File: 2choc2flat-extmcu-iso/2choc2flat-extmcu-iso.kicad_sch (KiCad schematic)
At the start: 142 parts, among them J1 Conn_01x09_Male, J2 Conn_01x05_Male, J3 Conn_01x09_Male, K1 KEYSW, K10 KEYSW, K11 KEYSW, K12 KEYSW, K13 KEYSW, K14 KEYSW, K15 KEYSW, K16 KEYSW, K17 KEYSW, K18 KEYSW, K19 KEYSW, K2 KEYSW, K20 KEYSW, K21 KEYSW, K22 KEYSW, K23 KEYSW, K24 KEYSW, K25 KEYSW, K26 KEYSW, K27 KEYSW, K28 KEYSW, K29 KEYSW, K29-1 KEYSW, K3 KEYSW, K30 KEYSW, K31 KEYSW, K32 KEYSW, K33 KEYSW, K34 KEYSW, K35 KEYSW, K36 KEYSW, K37 KEYSW, K38 KEYSW, K39 KEYSW, K4 KEYSW, K40 KEYSW, K41 KEYSW, K42 KEYSW, K43 KEYSW, K44 KEYSW, K45 KEYSW, K46 KEYSW, K47 KEYSW, K48 KEYSW, K49 KEYSW, K5 KEYSW, K50 KEYSW, K51 KEYSW, K52 KEYSW, K53 KEYSW, K54 KEYSW, K55 KEYSW, K56 KEYSW, K57 KEYSW, K58 KEYSW, K59 KEYSW, K6 KEYSW, K60 KEYSW, K61 KEYSW, K62 KEYSW, K63 KEYSW, K64 KEYSW, K65 KEYSW, K7 KEYSW, K8 KEYSW, K9 KEYSW

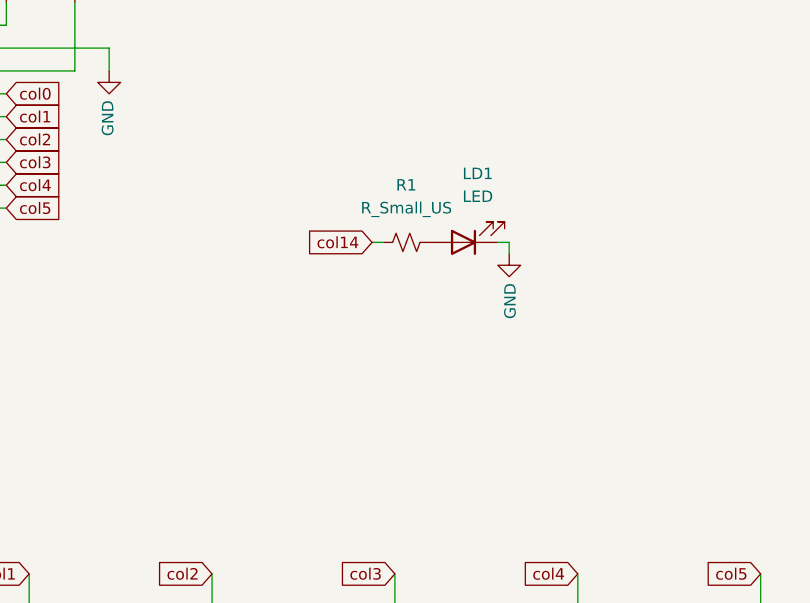
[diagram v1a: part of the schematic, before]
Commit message: add second caps led, minor tweaks
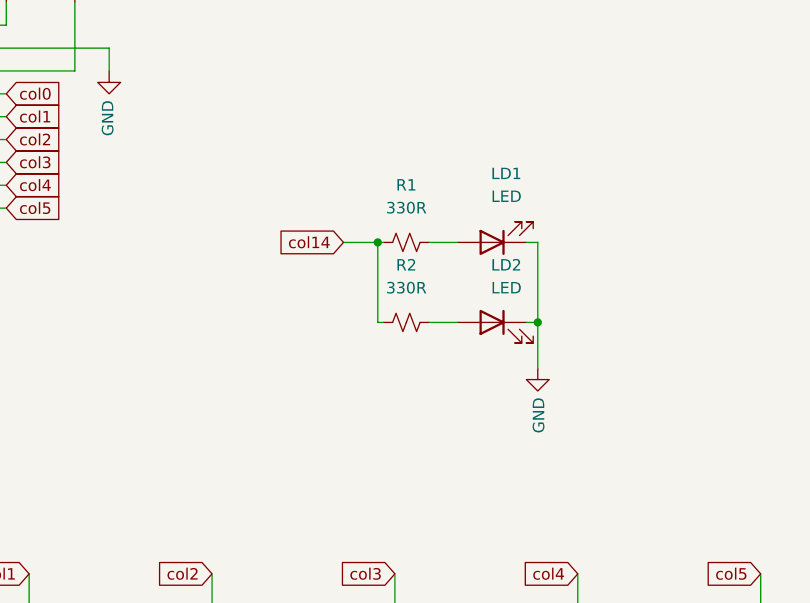
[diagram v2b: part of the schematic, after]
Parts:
- added LD2: LED, LED_SMD:LED_1206_3216Metric_ReverseMount_Hole1.8x2.4mm, symbol Device:LED
- added R2: 330R, Resistor_SMD:R_0603_1608Metric, symbol Device:R_Small_US
- R1: value R_Small_US -> 330R
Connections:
- net GND: now also LD2.1 (K)
- net col14: now also R2.1
- new net: LD2.2 (A), R2.2
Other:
- moved on the sheet: LD1
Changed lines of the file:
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@@
   (junction (at 311.15 189.23) (diameter 0) (color 0 0 0 0)
   )
+  (junction (at 161.925 80.01) (diameter 0) (color 0 0 0 0)
+  )
   (junction (at 168.91 168.91) (diameter 0) (color 0 0 0 0)
   )
@@
   (junction (at 148.59 133.35) (diameter 0) (color 0 0 0 0)
   )
+  (junction (at 144.145 71.12) (diameter 0) (color 0 0 0 0)
+  )
   (junction (at 250.19 189.23) (diameter 0) (color 0 0 0 0)
   )
@@
   (junction (at 288.29 123.19) (diameter 0) (color 0 0 0 0)
   )
+  (wire (pts (xy 144.145 71.12) (xy 144.145 80.01))
+    (stroke (width 0) (type default) (color 0 0 0 0))
+  )
   (wire (pts (xy 331.47 137.795) (xy 334.01 137.795))
     (stroke (width 0) (type default) (color 0 0 0 0))
@@
     (stroke (width 0) (type default) (color 0 0 0 0))
   )
+  (wire (pts (xy 160.655 80.01) (xy 161.925 80.01))
+    (stroke (width 0) (type default) (color 0 0 0 0))
+  )
   (wire (pts (xy 128.27 148.59) (xy 148.59 148.59))
     (stroke (width 0) (type default) (color 0 0 0 0))
@@
     (stroke (width 0) (type default) (color 0 0 0 0))
   )
+  (wire (pts (xy 161.925 80.01) (xy 161.925 85.09))
+    (stroke (width 0) (type default) (color 0 0 0 0))
+  )
   (wire (pts (xy 105.41 158.75) (xy 105.41 179.07))
     (stroke (width 0) (type default) (color 0 0 0 0))
@@
     (stroke (width 0) (type default) (color 0 0 0 0))
   )
-  (wire (pts (xy 157.48 71.12) (xy 158.75 71.12))
+  (wire (pts (xy 160.655 71.12) (xy 161.925 71.12))
     (stroke (width 0) (type default) (color 0 0 0 0))
   )
@@
     (stroke (width 0) (type default) (color 0 0 0 0))
   )
+  (wire (pts (xy 153.035 71.12) (xy 149.86 71.12))
+    (stroke (width 0) (type default) (color 0 0 0 0))
+  )
   (wire (pts (xy 270.51 209.55) (xy 250.19 209.55))
     (stroke (width 0) (type default) (color 0 0 0 0))
@@
     (stroke (width 0) (type default) (color 0 0 0 0))
   )
-  (wire (pts (xy 158.75 71.12) (xy 158.75 72.39))
+  (wire (pts (xy 161.925 71.12) (xy 161.925 80.01))
     (stroke (width 0) (type default) (color 0 0 0 0))
   )
@@
     (stroke (width 0) (type default) (color 0 0 0 0))
   )
+  (wire (pts (xy 144.145 71.12) (xy 144.78 71.12))
+    (stroke (width 0) (type default) (color 0 0 0 0))
+  )
   (wire (pts (xy 250.19 181.61) (xy 250.19 179.07))
     (stroke (width 0) (type default) (color 0 0 0 0))
@@
     (stroke (width 0) (type default) (color 0 0 0 0))
   )
-  (wire (pts (xy 143.51 71.12) (xy 144.78 71.12))
+  (wire (pts (xy 140.335 71.12) (xy 144.145 71.12))
     (stroke (width 0) (type default) (color 0 0 0 0))
   )
@@
     (stroke (width 0) (type default) (color 0 0 0 0))
   )
+  (wire (pts (xy 149.86 80.01) (xy 153.035 80.01))
+    (stroke (width 0) (type default) (color 0 0 0 0))
+  )
   (wire (pts (xy 209.55 125.73) (xy 209.55 123.19))
     (stroke (width 0) (type default) (color 0 0 0 0))
@@
     (stroke (width 0) (type default) (color 0 0 0 0))
   )
+  (wire (pts (xy 144.145 80.01) (xy 144.78 80.01))
+    (stroke (width 0) (type default) (color 0 0 0 0))
+  )
   (wire (pts (xy 87.63 138.43) (xy 90.17 138.43))
     (stroke (width 0) (type default) (color 0 0 0 0))
@@
     )
   )
-  (global_label "col14" (shape input) (at 143.51 71.12 180)
+  (global_label "col14" (shape input) (at 140.335 71.12 180)
     (effects (font (size 1.27 1.27)) (justify right))
-    (property "Intersheet References" "${INTERSHEET_REFS}" (id 0) (at -187.96 -59.69 0)
+    (property "Intersheet References" "${INTERSHEET_REFS}" (id 0) (at -191.135 -59.69 0)
       (effects (font (size 1.27 1.27)) hide)
     )
@@
     (pin "1")
   )
-  (symbol (lib_id "Power:GND") (at 158.75 72.39 0) (unit 1)
+  (symbol (lib_id "Power:GND") (at 161.925 85.09 0) (unit 1)
     (in_bom yes) (on_board yes)
-    (property "Reference" "#PWR0103" (id 0) (at 158.75 78.74 0)
+    (property "Reference" "#PWR0103" (id 0) (at 161.925 91.44 0)
       (effects (font (size 1.27 1.27)) hide)
     )
-    (property "Value" "GND" (id 1) (at 158.877 75.6412 90)
+    (property "Value" "GND" (id 1) (at 162.052 88.3412 90)
       (effects (font (size 1.27 1.27)) (justify right))
     )
-    (property "Footprint" "" (id 2) (at 158.75 72.39 0)
+    (property "Footprint" "" (id 2) (at 161.925 85.09 0)
       (effects (font (size 1.27 1.27)) hide)
     )
-    (property "Datasheet" "" (id 3) (at 158.75 72.39 0)
+    (property "Datasheet" "" (id 3) (at 161.925 85.09 0)
       (effects (font (size 1.27 1.27)) hide)
     )
@@
     (in_bom yes) (on_board yes) (fields_autoplaced)
     (property "Reference" "R1" (id 0) (at 147.32 64.77 90))
-    (property "Value" "R_Small_US" (id 1) (at 147.32 67.31 90))
+    (property "Value" "330R" (id 1) (at 147.32 67.31 90))
     (property "Footprint" "Resistor_SMD:R_0603_1608Metric" (id 2) (at 147.32 71.12 0)
       (effects (font (size 1.27 1.27)) hide)
@@
     (pin "2")
   )
-  (symbol (lib_id "Device:LED") (at 153.67 71.12 180) (unit 1)
+  (symbol (lib_id "Device:LED") (at 156.845 71.12 180) (unit 1)
+    (in_bom yes) (on_board yes) (fields_autoplaced)
+    (property "Reference" "LD1" (id 0) (at 158.4325 63.5 0))
+    (property "Value" "LED" (id 1) (at 158.4325 66.04 0))
+    (property "Footprint" "LED_SMD:LED_1206_3216Metric_ReverseMount_Hole1.8x2.4mm" (id 2) (at 156.845 71.12 0)
+      (effects (font (size 1.27 1.27)) hide)
+    )
+    (property "Datasheet" "~" (id 3) (at 156.845 71.12 0)
+      (effects (font (size 1.27 1.27)) hide)
+    )
+    (pin "1")
+    (pin "2")
+  )
+  (symbol (lib_id "Device:R_Small_US") (at 147.32 80.01 90) (unit 1)
     (in_bom yes) (on_board yes) (fields_autoplaced)
-    (property "Reference" "LD1" (id 0) (at 155.2575 63.5 0))
-    (property "Value" "LED" (id 1) (at 155.2575 66.04 0))
-    (property "Footprint" "LED_SMD:LED_1206_3216Metric_ReverseMount_Hole1.8x2.4mm" (id 2) (at 153.67 71.12 0)
+    (property "Reference" "R2" (id 0) (at 147.32 73.66 90))
+    (property "Value" "330R" (id 1) (at 147.32 76.2 90))
+    (property "Footprint" "Resistor_SMD:R_0603_1608Metric" (id 2) (at 147.32 80.01 0)
       (effects (font (size 1.27 1.27)) hide)
     )
-    (property "Datasheet" "~" (id 3) (at 153.67 71.12 0)
+    (property "Datasheet" "~" (id 3) (at 147.32 80.01 0)
+      (effects (font (size 1.27 1.27)) hide)
+    )
+    (pin "1")
+    (pin "2")
+  )
+  (symbol (lib_id "Device:LED") (at 156.845 80.01 0) (mirror y) (unit 1)
+    (in_bom yes) (on_board yes)
+    (property "Reference" "LD2" (id 0) (at 158.4325 73.66 0))
+    (property "Value" "LED" (id 1) (at 158.4325 76.2 0))
+    (property "Footprint" "LED_SMD:LED_1206_3216Metric_ReverseMount_Hole1.8x2.4mm" (id 2) (at 156.845 80.01 0)
+      (effects (font (size 1.27 1.27)) hide)
+    )
+    (property "Datasheet" "~" (id 3) (at 156.845 80.01 0)
       (effects (font (size 1.27 1.27)) hide)
     )
@@
       (reference "LD1") (unit 1) (value "LED") (footprint "LED_SMD:LED_1206_3216Metric_ReverseMount_Hole1.8x2.4mm")
     )
+    (path "/c9114b6f-4d02-4a79-8f9e-f80a96726ab0"
+      (reference "LD2") (unit 1) (value "LED") (footprint "LED_SMD:LED_1206_3216Metric_ReverseMount_Hole1.8x2.4mm")
+    )
     (path "/3fec37d1-4a02-4de4-982c-f6d5d4781efb"
-      (reference "R1") (unit 1) (value "R_Small_US") (footprint "Resistor_SMD:R_0603_1608Metric")
+      (reference "R1") (unit 1) (value "330R") (footprint "Resistor_SMD:R_0603_1608Metric")
+    )
+    (path "/c84f7357-ba09-468d-8a79-98228254bd2d"
+      (reference "R2") (unit 1) (value "330R") (footprint "Resistor_SMD:R_0603_1608Metric")
     )
     (path "/00000000-0000-0000-0000-00005c2a7b35"

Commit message: whoops wip
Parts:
- K42: footprint Switch_Keyboard_Hotswap_Kailh_mine:SW_Hotswap_Kailh_Choc_V2_ISOEnter_Gateron_LP_Stabs -> Switch_Keyboard_Hotswap_Kailh_mine:SW_Hotswap_Kailh_Choc_V2_ISOEnter_West_Gateron_LP_Stabs
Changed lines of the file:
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@@
       (effects (font (size 1.524 1.524)) hide)
     )
-    (property "Footprint" "Switch_Keyboard_Hotswap_Kailh_mine:SW_Hotswap_Kailh_Choc_V2_ISOEnter_Gateron_LP_Stabs" (id 2) (at 341.63 158.75 0)
+    (property "Footprint" "Switch_Keyboard_Hotswap_Kailh_mine:SW_Hotswap_Kailh_Choc_V2_ISOEnter_West_Gateron_LP_Stabs" (id 2) (at 341.63 158.75 0)
       (effects (font (size 1.524 1.524)) hide)
     )
@@
     )
     (path "/00000000-0000-0000-0000-00005c818730"
-      (reference "K42") (unit 1) (value "KEYSW") (footprint "Switch_Keyboard_Hotswap_Kailh_mine:SW_Hotswap_Kailh_Choc_V2_ISOEnter_Gateron_LP_Stabs")
+      (reference "K42") (unit 1) (value "KEYSW") (footprint "Switch_Keyboard_Hotswap_Kailh_mine:SW_Hotswap_Kailh_Choc_V2_ISOEnter_West_Gateron_LP_Stabs")
     )
     (path "/00000000-0000-0000-0000-00005c5435b9"

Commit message: version 1.4 with foam layers on eco1 and eco2
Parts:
- LD1, LD2: footprint LED_SMD:LED_1206_3216Metric_ReverseMount_Hole1.8x2.4mm -> schizobovine:LED_1206_3216Metric_ReverseMount_Hole1.8x2.4mm
- R1, R2: footprint Resistor_SMD:R_0603_1608Metric -> schizobovine:R_0603_1608Metric
- S1, S2, S6: footprint footprints:5.5_5x2.5mm -> schizobovine:3_5x2.5mm
- S3: footprint MountingHole:MountingHole_2.2mm_M2_Pad_TopOnly -> schizobovine:MountingHole_2.2mm_M2_Pad_TopOnly
- S4, S5: footprint footprints:10x5_7x2.5mm -> schizobovine:8x3.5_7x2.5mm
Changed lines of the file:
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@@
       (effects (font (size 1.27 1.27)) (justify left))
     )
-    (property "Footprint" "footprints:5.5_5x2.5mm" (id 2) (at 234.95 25.4 0)
+    (property "Footprint" "schizobovine:3_5x2.5mm" (id 2) (at 234.95 25.4 0)
       (effects (font (size 1.27 1.27)) hide)
     )
@@
       (effects (font (size 1.27 1.27)) (justify left))
     )
-    (property "Footprint" "footprints:5.5_5x2.5mm" (id 2) (at 234.95 31.75 0)
+    (property "Footprint" "schizobovine:3_5x2.5mm" (id 2) (at 234.95 31.75 0)
       (effects (font (size 1.27 1.27)) hide)
     )
@@
       (effects (font (size 1.27 1.27)) (justify left))
     )
-    (property "Footprint" "MountingHole:MountingHole_2.2mm_M2_Pad_TopOnly" (id 2) (at 234.95 38.1 0)
+    (property "Footprint" "schizobovine:MountingHole_2.2mm_M2_Pad_TopOnly" (id 2) (at 234.95 38.1 0)
       (effects (font (size 1.27 1.27)) hide)
     )
@@
       (effects (font (size 1.27 1.27)) (justify left))
     )
-    (property "Footprint" "footprints:10x5_7x2.5mm" (id 2) (at 234.95 44.45 0)
+    (property "Footprint" "schizobovine:8x3.5_7x2.5mm" (id 2) (at 234.95 44.45 0)
       (effects (font (size 1.27 1.27)) hide)
     )
@@
       (effects (font (size 1.27 1.27)) (justify left))
     )
-    (property "Footprint" "footprints:10x5_7x2.5mm" (id 2) (at 234.95 50.8 0)
+    (property "Footprint" "schizobovine:8x3.5_7x2.5mm" (id 2) (at 234.95 50.8 0)
       (effects (font (size 1.27 1.27)) hide)
     )
@@
       (effects (font (size 1.27 1.27)) (justify left))
     )
-    (property "Footprint" "footprints:5.5_5x2.5mm" (id 2) (at 234.95 57.15 0)
+    (property "Footprint" "schizobovine:3_5x2.5mm" (id 2) (at 234.95 57.15 0)
       (effects (font (size 1.27 1.27)) hide)
     )
@@
     (property "Reference" "R1" (id 0) (at 147.32 64.77 90))
     (property "Value" "330R" (id 1) (at 147.32 67.31 90))
-    (property "Footprint" "Resistor_SMD:R_0603_1608Metric" (id 2) (at 147.32 71.12 0)
+    (property "Footprint" "schizobovine:R_0603_1608Metric" (id 2) (at 147.32 71.12 0)
       (effects (font (size 1.27 1.27)) hide)
     )
@@
     (property "Reference" "LD1" (id 0) (at 158.4325 63.5 0))
     (property "Value" "LED" (id 1) (at 158.4325 66.04 0))
-    (property "Footprint" "LED_SMD:LED_1206_3216Metric_ReverseMount_Hole1.8x2.4mm" (id 2) (at 156.845 71.12 0)
+    (property "Footprint" "schizobovine:LED_1206_3216Metric_ReverseMount_Hole1.8x2.4mm" (id 2) (at 156.845 71.12 0)
       (effects (font (size 1.27 1.27)) hide)
     )
@@
     (property "Reference" "R2" (id 0) (at 147.32 73.66 90))
     (property "Value" "330R" (id 1) (at 147.32 76.2 90))
-    (property "Footprint" "Resistor_SMD:R_0603_1608Metric" (id 2) (at 147.32 80.01 0)
+    (property "Footprint" "schizobovine:R_0603_1608Metric" (id 2) (at 147.32 80.01 0)
       (effects (font (size 1.27 1.27)) hide)
     )
@@
     (property "Reference" "LD2" (id 0) (at 158.4325 73.66 0))
     (property "Value" "LED" (id 1) (at 158.4325 76.2 0))
-    (property "Footprint" "LED_SMD:LED_1206_3216Metric_ReverseMount_Hole1.8x2.4mm" (id 2) (at 156.845 80.01 0)
+    (property "Footprint" "schizobovine:LED_1206_3216Metric_ReverseMount_Hole1.8x2.4mm" (id 2) (at 156.845 80.01 0)
       (effects (font (size 1.27 1.27)) hide)
     )
@@
     )
     (path "/c0bcce99-3568-4911-a31f-2e9713a455b2"
-      (reference "LD1") (unit 1) (value "LED") (footprint "LED_SMD:LED_1206_3216Metric_ReverseMount_Hole1.8x2.4mm")
+      (reference "LD1") (unit 1) (value "LED") (footprint "schizobovine:LED_1206_3216Metric_ReverseMount_Hole1.8x2.4mm")
     )
     (path "/c9114b6f-4d02-4a79-8f9e-f80a96726ab0"
-      (reference "LD2") (unit 1) (value "LED") (footprint "LED_SMD:LED_1206_3216Metric_ReverseMount_Hole1.8x2.4mm")
+      (reference "LD2") (unit 1) (value "LED") (footprint "schizobovine:LED_1206_3216Metric_ReverseMount_Hole1.8x2.4mm")
     )
     (path "/3fec37d1-4a02-4de4-982c-f6d5d4781efb"
-      (reference "R1") (unit 1) (value "330R") (footprint "Resistor_SMD:R_0603_1608Metric")
+      (reference "R1") (unit 1) (value "330R") (footprint "schizobovine:R_0603_1608Metric")
     )
     (path "/c84f7357-ba09-468d-8a79-98228254bd2d"
-      (reference "R2") (unit 1) (value "330R") (footprint "Resistor_SMD:R_0603_1608Metric")
+      (reference "R2") (unit 1) (value "330R") (footprint "schizobovine:R_0603_1608Metric")
     )
     (path "/00000000-0000-0000-0000-00005c2a7b35"
-      (reference "S1") (unit 1) (value "Screw") (footprint "footprints:5.5_5x2.5mm")
+      (reference "S1") (unit 1) (value "Screw") (footprint "schizobovine:3_5x2.5mm")
     )
     (path "/00000000-0000-0000-0000-00005c2aa553"
-      (reference "S2") (unit 1) (value "Screw") (footprint "footprints:5.5_5x2.5mm")
+      (reference "S2") (unit 1) (value "Screw") (footprint "schizobovine:3_5x2.5mm")
     )
     (path "/00000000-0000-0000-0000-00005c2cd859"
-      (reference "S3") (unit 1) (value "Screw") (footprint "MountingHole:MountingHole_2.2mm_M2_Pad_TopOnly")
+      (reference "S3") (unit 1) (value "Screw") (footprint "schizobovine:MountingHole_2.2mm_M2_Pad_TopOnly")
     )
     (path "/00000000-0000-0000-0000-00005c2f0889"
-      (reference "S4") (unit 1) (value "Screw") (footprint "footprints:10x5_7x2.5mm")
+      (reference "S4") (unit 1) (value "Screw") (footprint "schizobovine:8x3.5_7x2.5mm")
     )
     (path "/00000000-0000-0000-0000-00005c313929"
-      (reference "S5") (unit 1) (value "Screw") (footprint "footprints:10x5_7x2.5mm")
+      (reference "S5") (unit 1) (value "Screw") (footprint "schizobovine:8x3.5_7x2.5mm")
     )
     (path "/00000000-0000-0000-0000-00005c3372c8"
-      (reference "S6") (unit 1) (value "Screw") (footprint "footprints:5.5_5x2.5mm")
+      (reference "S6") (unit 1) (value "Screw") (footprint "schizobovine:3_5x2.5mm")
     )
   )
